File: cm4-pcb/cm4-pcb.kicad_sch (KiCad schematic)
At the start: 25 parts, among them J1 Conn_01x02_Pin, J2 Conn_01x02_Pin, U1 Pfostenstecker_6_2x3, U2 Pfostenstecker_6_2x3, U3 Pfostenstecker_6_2x3, U4 MagJack-A70-112-331N126, U5 SMD-PUSH-BTN

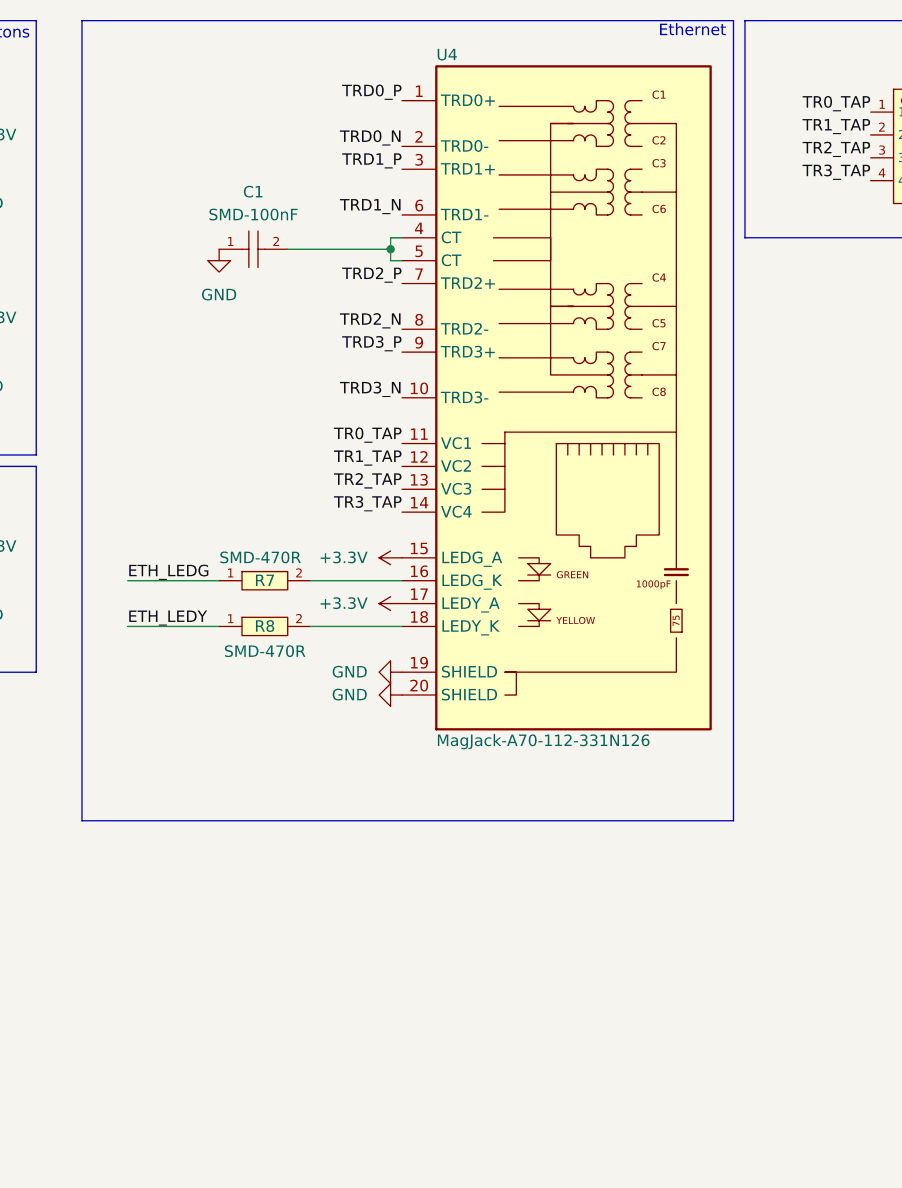
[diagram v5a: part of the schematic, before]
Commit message: Added USB Connector
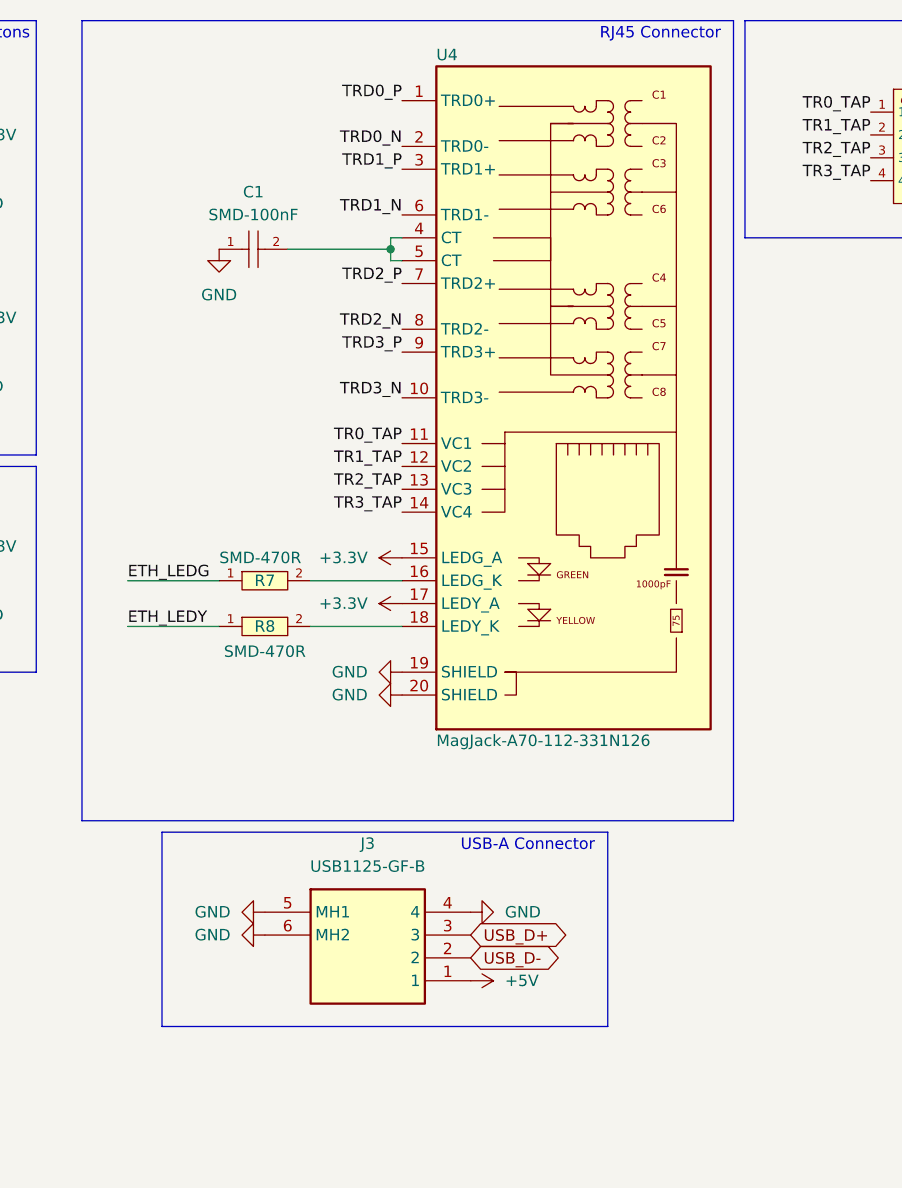
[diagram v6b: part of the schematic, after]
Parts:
- added J3: USB1125-GF-B, USB1125GFB, symbol USB1125-GF-B:USB1125-GF-B
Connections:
- net +5V: now also J3.1
- net GND: now also J3.4, J3.5 (MH1), J3.6 (MH2)
- net USB_D+: now also J3.3
- net USB_D-: now also J3.2
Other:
- note added: "RJ45 Connector"
- note added: "USB-A Connector"
- note removed: "Ethernet"

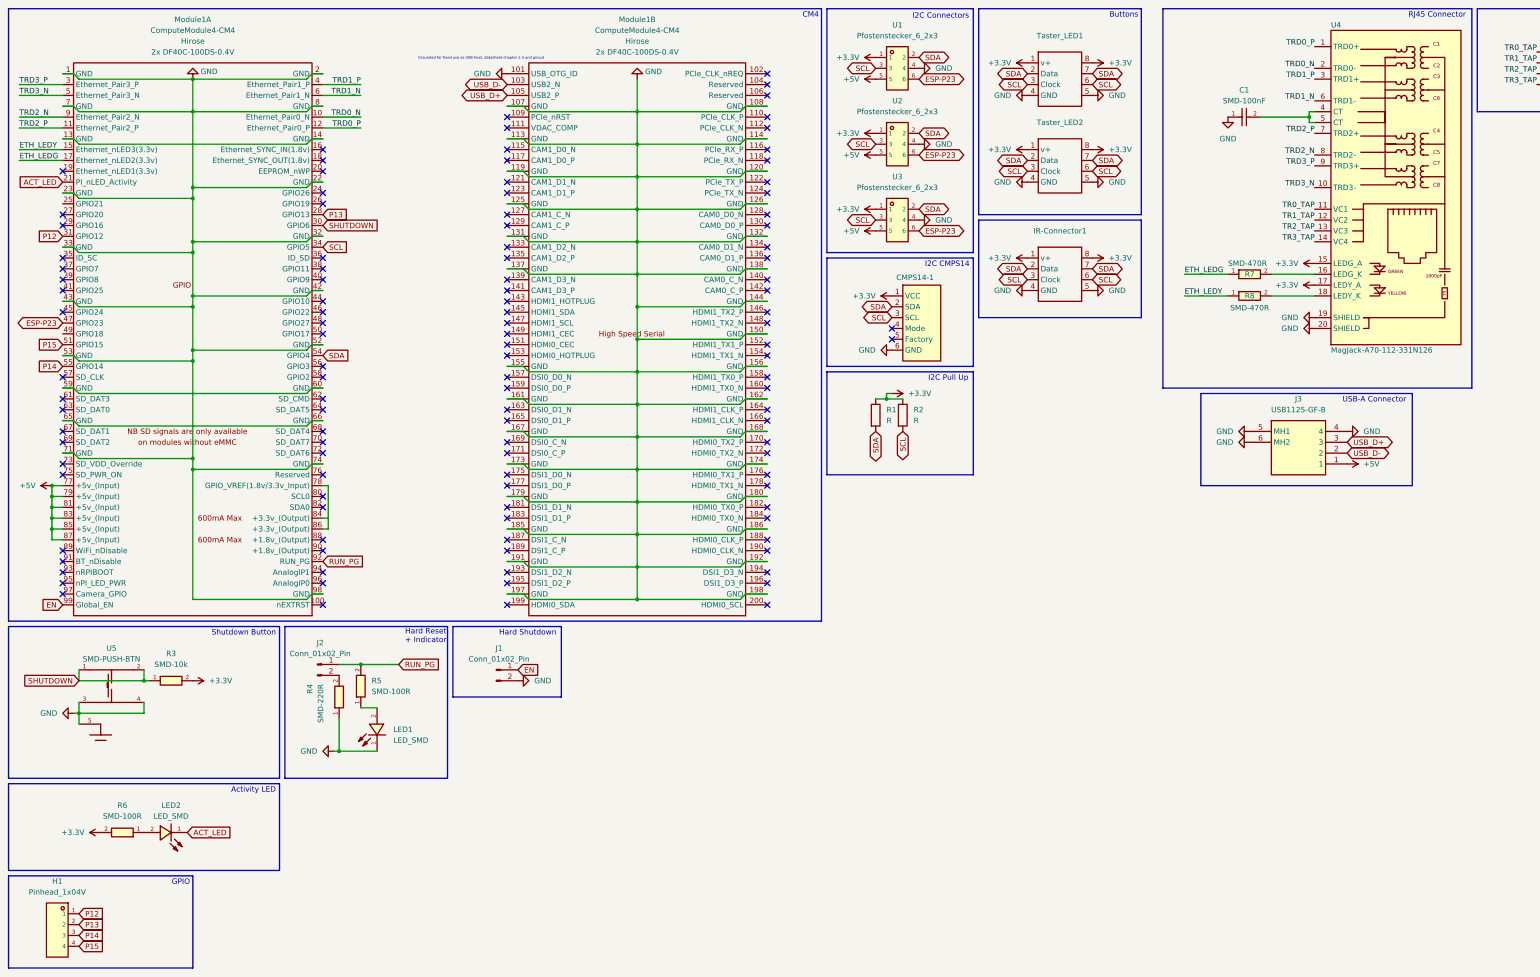
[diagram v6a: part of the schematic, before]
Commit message: Added Power Flags + set ERC Rules
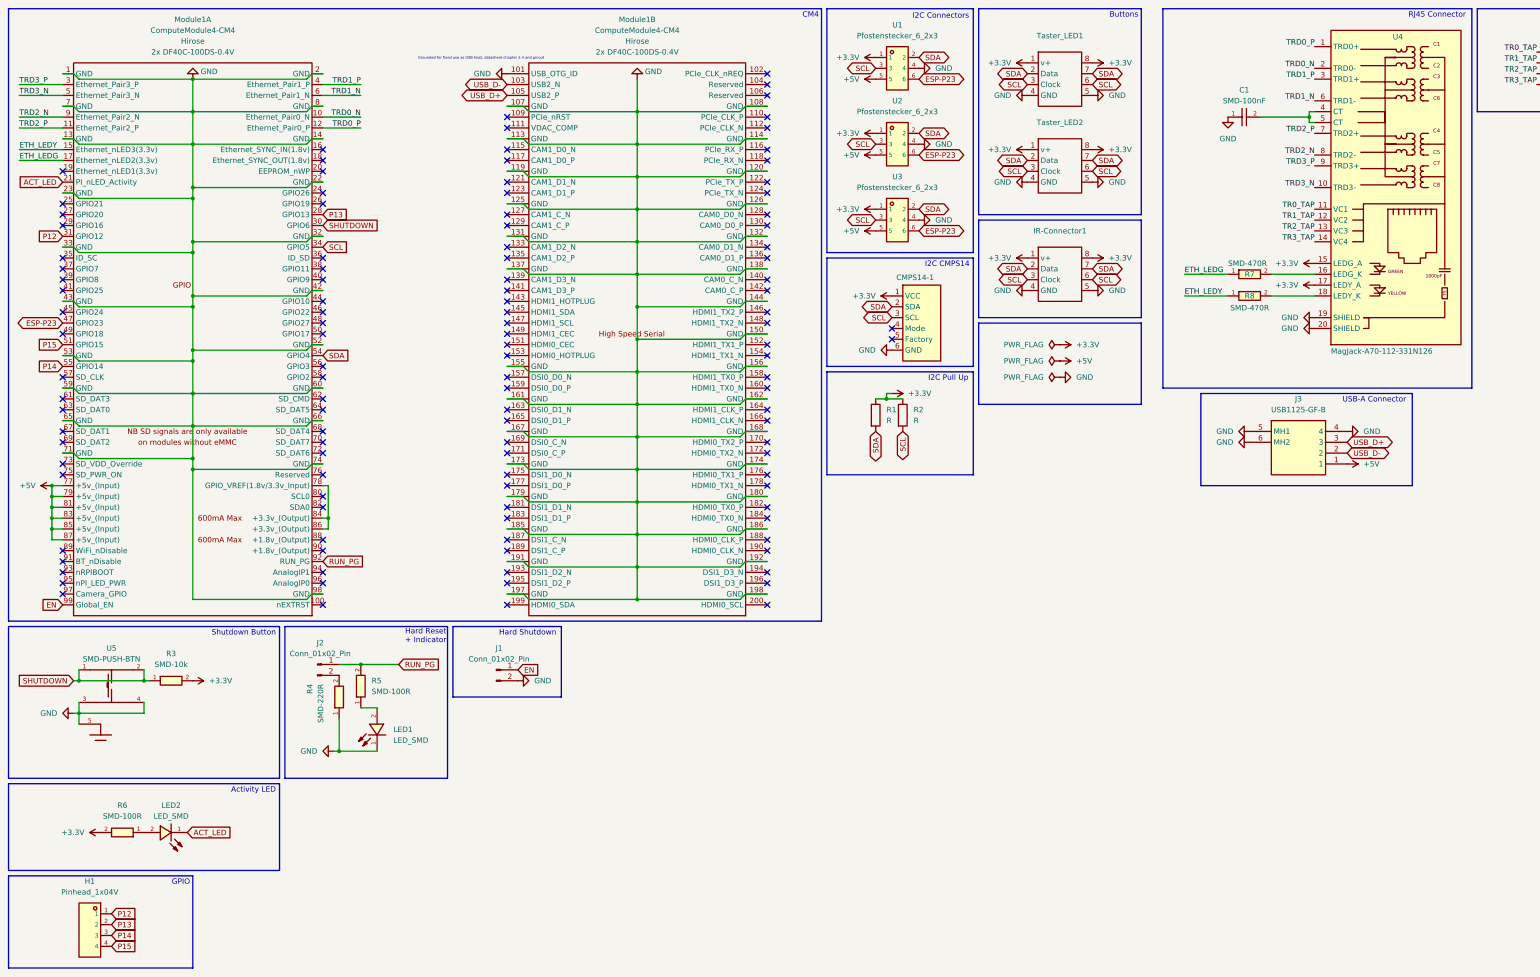
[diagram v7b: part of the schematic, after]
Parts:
- U4: footprint CM4IO:TRJG0926HENL -> (none); Field6 TRJG0926HENL -> (none); Field7 Trxcon -> (none); Field8 UCON00900 -> (none); Part Description Gigabit Ethernet Magjack -> (none)
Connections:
- net GND: now also Module1.13 (GND), Module1.14 (GND), Module1.59 (GND), Module1.60 (GND), Module1.65 (GND), Module1.66 (GND)
- net at Module1.78 (GPIO_VREF(1.8v/3.3v_Input)), Module1.86 (+3.3v_(Output)): now also Module1.84 (+3.3v_(Output))
- no-connect marks 116 -> 118
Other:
- moved on the sheet: H1

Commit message: PCB Placement
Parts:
- removed IR-Connector1: ~, BohleBots:TASTER_LED, symbol bohlebots.lib:Taster_Led
- removed U3: Pfostenstecker_6_2x3, BohleBots:HDR-TH_6P-P2.54-V-F-R2-C3-S2.54-4, symbol bohlebots.lib:Pfostenstecker_6_2x3
- added C2: SMD-1uF, BohleBots:C0603, symbol bohlebots.lib:SMD-1uF
- added H3, H4, H5, H6: MountingHole, BohleBots:MountingHole_4.3mm_M4, symbol bohlebots.lib:MountingHole
- added J4: Conn_02x03_Odd_Even, Connector_PinHeader_2.54mm:PinHeader_2x03_P2.54mm_Vertical, symbol Connector_Generic:Conn_02x03_Odd_Even
- U4: footprint (none) -> CM4IO:TRJG0926HENL
- renumbered LED2 to ACT_LED1, LED1 to RUN_LED1
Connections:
- net +3.3V: now also J4.2 (Pin_2)
- net GND: now also C2.2, J4.3 (Pin_3)
- net SCL: now also J4.4 (Pin_4)
- net SDA: now also J4.1 (Pin_1)
- net SHUTDOWN: now also C2.1
- no-connect marks 118 -> 120
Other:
- note added: "IR-Connector"
- moved on the sheet: CMPS14-1, R1, R2, R3
